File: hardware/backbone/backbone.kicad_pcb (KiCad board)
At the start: 4 copper layers, 31.3 x 68.9 mm, 75 parts, among them J1 M20-7810645R, J140 M20-7810645R, J2 FROM_PREVIOUS, J3 M20-7810645R, J4 SM04B-SRSS-TB(LF)(SN), J5 FH12-24S-0.5SH(55), J9 TO NEXT, Q2 AO3401A, U1 ESP32-S3-WROOM-1_1U_FlexyPin_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, U2 SN65HVD230DR, U3 HC-TYPE-C-16P-01A, U4 TPS562201DDCR, U8 G3VM-61VY3

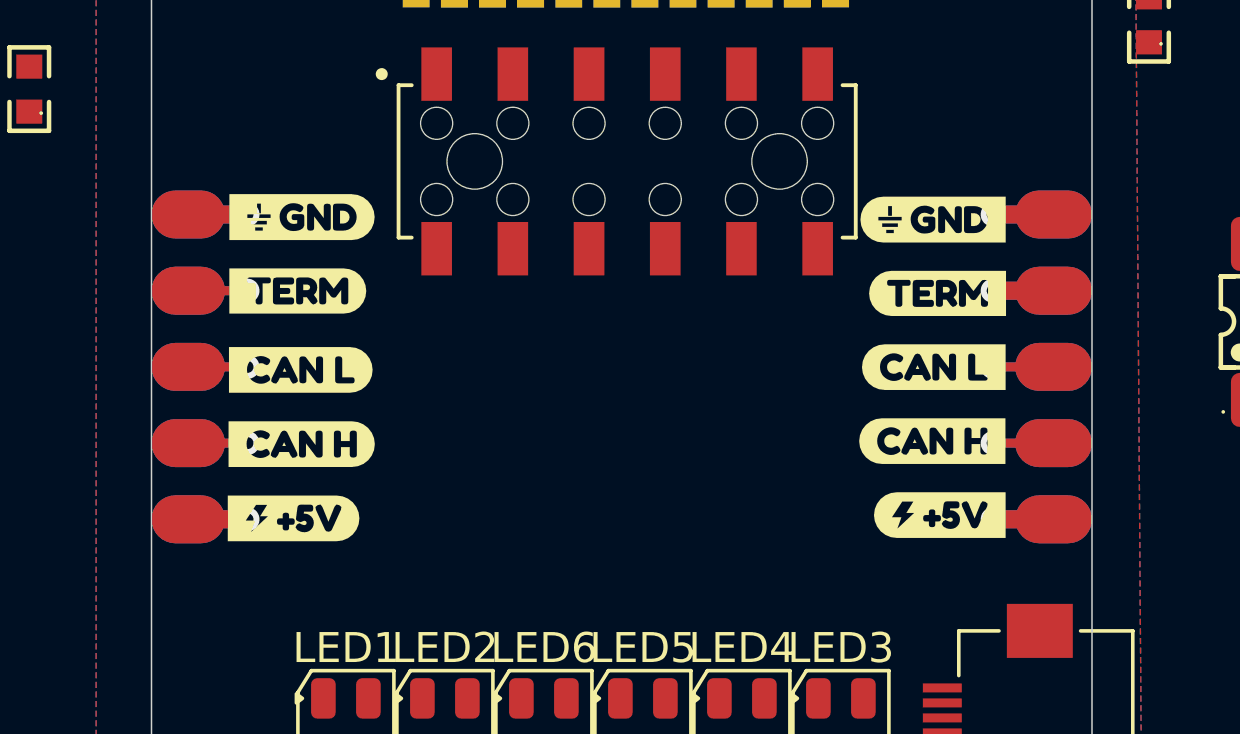
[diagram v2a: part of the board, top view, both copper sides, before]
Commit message: Reinforce magnetic connector power and ground layer transitions
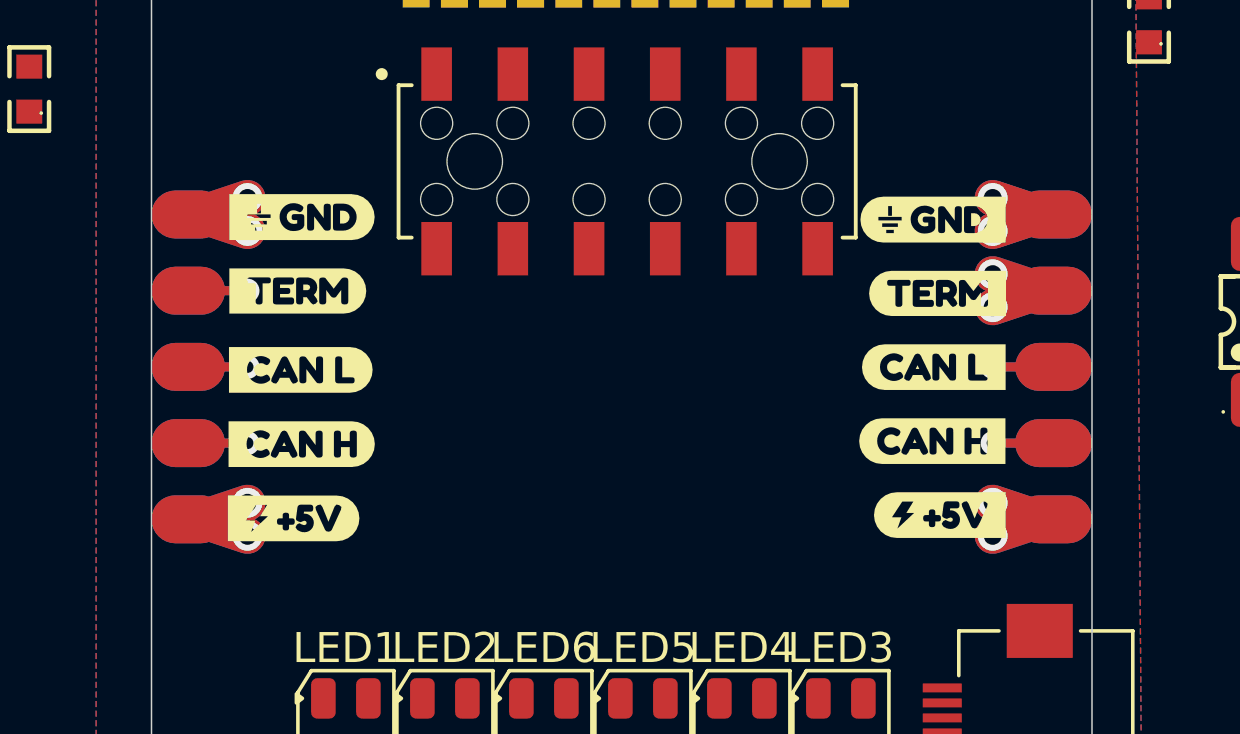
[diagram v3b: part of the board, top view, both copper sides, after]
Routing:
- net 5V: track 9.90 -> 20.9 mm, vias 3 -> 6
- net GND: track 6.60 -> 13.9 mm, vias 2 -> 4
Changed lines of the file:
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@@
 (footprint "Resistor_SMD:R_0603_1608Metric" (layer "F.Cu") (descr "Resistor SMD 0603 (1608 Metric), square (rectangular) end terminal, IPC-7351 nominal, (Body size source: IPC-SM-782 page 72, https://www.pcb-3d.com/wordpress/wp-content/uploads/ipc-sm-782a_amendment_1_and_2.pdf)") (tags "resistor") (property "Reference" "R36" (at 0 -1.43 0) (layer "F.SilkS") (effects (font (size 1 1) (thickness 0.15)))) (property "Value" "33k 1%" (at 0 1.43 0) (layer "F.Fab") (effects (font (size 1 1) (thickness 0.15))) (hide yes)) (property "KiLib_Generator" "SMD_2terminal_chip_molded" (at 0 0 0) (layer "F.SilkS") (hide yes) (effects (font (size 1 1) (thickness 0.15)))) (attr smd) (duplicate_pad_numbers_are_jumpers no) (fp_line (start -0.237258 -0.5225) (end 0.237258 -0.5225) (stroke (width 0.12) (type solid)) (layer "F.SilkS")) (fp_line (start -0.237258 0.5225) (end 0.237258 0.5225) (stroke (width 0.12) (type solid)) (layer "F.SilkS")) (fp_rect (start -1.48 -0.73) (end 1.48 0.73) (stroke (width 0.05) (type solid)) (fill no) (layer "F.CrtYd")) (fp_rect (start -0.8 -0.4125) (end 0.8 0.4125) (stroke (width 0.1) (type solid)) (fill no) (layer "F.Fab")) (fp_text user "${REFERENCE}" (at 0 0 0) (layer "F.Fab") (effects (font (size 0.4 0.4) (thickness 0.06)))) (pad "1" smd roundrect (at -0.825 0) (size 0.8 0.95) (layers "F.Cu" "F.Mask" "F.Paste") (roundrect_rratio 0.25) (net "VCORE")) (pad "2" smd roundrect (at 0.825 0) (size 0.8 0.95) (layers "F.Cu" "F.Mask" "F.Paste") (roundrect_rratio 0.25) (net "Net-(U4-VFB)")) (embedded_fonts no) (model "${KICAD10_3DMODEL_DIR}/Resistor_SMD.3dshapes/R_0603_1608Metric.step" (offset (xyz 0 0 0)) (scale (xyz 1 1 1)) (rotate (xyz 0 0 0))) (at 243 86) (property "MPN" "0603WAF3302T5E" (at 0 0 0) (layer "F.Fab") (hide yes) (effects (font (size 1 1) (thickness 0.15)))) (property "LCSC Part" "C4216" (at 0 0 0) (layer "F.Fab") (hide yes) (effects (font (size 1 1) (thickness 0.15)))))
 (footprint "Resistor_SMD:R_0603_1608Metric" (layer "F.Cu") (descr "Resistor SMD 0603 (1608 Metric), square (rectangular) end terminal, IPC-7351 nominal, (Body size source: IPC-SM-782 page 72, https://www.pcb-3d.com/wordpress/wp-content/uploads/ipc-sm-782a_amendment_1_and_2.pdf)") (tags "resistor") (property "Reference" "R37" (at 0 -1.43 0) (layer "F.SilkS") (effects (font (size 1 1) (thickness 0.15)))) (property "Value" "10k 1%" (at 0 1.43 0) (layer "F.Fab") (effects (font (size 1 1) (thickness 0.15))) (hide yes)) (property "KiLib_Generator" "SMD_2terminal_chip_molded" (at 0 0 0) (layer "F.SilkS") (hide yes) (effects (font (size 1 1) (thickness 0.15)))) (attr smd) (duplicate_pad_numbers_are_jumpers no) (fp_line (start -0.237258 -0.5225) (end 0.237258 -0.5225) (stroke (width 0.12) (type solid)) (layer "F.SilkS")) (fp_line (start -0.237258 0.5225) (end 0.237258 0.5225) (stroke (width 0.12) (type solid)) (layer "F.SilkS")) (fp_rect (start -1.48 -0.73) (end 1.48 0.73) (stroke (width 0.05) (type solid)) (fill no) (layer "F.CrtYd")) (fp_rect (start -0.8 -0.4125) (end 0.8 0.4125) (stroke (width 0.1) (type solid)) (fill no) (layer "F.Fab")) (fp_text user "${REFERENCE}" (at 0 0 0) (layer "F.Fab") (effects (font (size 0.4 0.4) (thickness 0.06)))) (pad "1" smd roundrect (at -0.825 0) (size 0.8 0.95) (layers "F.Cu" "F.Mask" "F.Paste") (roundrect_rratio 0.25) (net "Net-(U4-VFB)")) (pad "2" smd roundrect (at 0.825 0) (size 0.8 0.95) (layers "F.Cu" "F.Mask" "F.Paste") (roundrect_rratio 0.25) (net "GND")) (embedded_fonts no) (model "${KICAD10_3DMODEL_DIR}/Resistor_SMD.3dshapes/R_0603_1608Metric.step" (offset (xyz 0 0 0)) (scale (xyz 1 1 1)) (rotate (xyz 0 0 0))) (at 251 86) (property "MPN" "0603WAF1002T5E" (at 0 0 0) (layer "F.Fab") (hide yes) (effects (font (size 1 1) (thickness 0.15)))) (property "LCSC Part" "C25804" (at 0 0 0) (layer "F.Fab") (hide yes) (effects (font (size 1 1) (thickness 0.15)))))
-(via (at 179.940 102.130) (size 0.8) (drill 0.4) (layers "F.Cu" "B.Cu") (net "5V"))
-(segment (start 181.590 102.130) (end 179.940 102.130) (width 0.6) (layer "F.Cu") (net "5V"))
-(segment (start 181.590 102.130) (end 179.940 102.130) (width 0.6) (layer "B.Cu") (net "5V"))
+(via (at 179.940 101.58) (size 1.0) (drill 0.6) (layers "F.Cu" "B.Cu") (net "5V"))
+(segment (start 181.590 102.130) (end 179.940 101.58) (width 1.2) (layer "F.Cu") (net "5V"))
+(segment (start 181.590 102.130) (end 179.940 101.58) (width 1.2) (layer "B.Cu") (net "5V"))
 (via (at 179.940 99.590) (size 0.8) (drill 0.4) (layers "F.Cu" "B.Cu") (net "CAN_H"))
 (segment (start 181.590 99.590) (end 179.940 99.590) (width 0.3) (layer "F.Cu") (net "CAN_H"))
@@
 (segment (start 181.590 97.050) (end 179.940 97.050) (width 0.3) (layer "F.Cu") (net "CAN_L"))
 (segment (start 181.590 97.050) (end 179.940 97.050) (width 0.3) (layer "B.Cu") (net "CAN_L"))
-(via (at 179.940 94.510) (size 0.8) (drill 0.4) (layers "F.Cu" "B.Cu") (net "5V"))
-(segment (start 181.590 94.510) (end 179.940 94.510) (width 0.6) (layer "F.Cu") (net "5V"))
-(segment (start 181.590 94.510) (end 179.940 94.510) (width 0.6) (layer "B.Cu") (net "5V"))
-(via (at 179.940 91.970) (size 0.8) (drill 0.4) (layers "F.Cu" "B.Cu") (net "GND"))
-(segment (start 181.590 91.970) (end 179.940 91.970) (width 0.6) (layer "F.Cu") (net "GND"))
-(segment (start 181.590 91.970) (end 179.940 91.970) (width 0.6) (layer "B.Cu") (net "GND"))
-(via (at 155.100 102.130) (size 0.8) (drill 0.4) (layers "F.Cu" "B.Cu") (net "5V"))
-(segment (start 153.450 102.130) (end 155.100 102.130) (width 0.6) (layer "F.Cu") (net "5V"))
-(segment (start 153.450 102.130) (end 155.100 102.130) (width 0.6) (layer "B.Cu") (net "5V"))
+(via (at 179.940 93.96) (size 1.0) (drill 0.6) (layers "F.Cu" "B.Cu") (net "5V"))
+(segment (start 181.590 94.510) (end 179.940 93.96) (width 1.2) (layer "F.Cu") (net "5V"))
+(segment (start 181.590 94.510) (end 179.940 93.96) (width 1.2) (layer "B.Cu") (net "5V"))
+(via (at 179.940 91.42) (size 1.0) (drill 0.6) (layers "F.Cu" "B.Cu") (net "GND"))
+(segment (start 181.590 91.970) (end 179.940 91.42) (width 1.2) (layer "F.Cu") (net "GND"))
+(segment (start 181.590 91.970) (end 179.940 91.42) (width 1.2) (layer "B.Cu") (net "GND"))
+(via (at 155.100 101.58) (size 1.0) (drill 0.6) (layers "F.Cu" "B.Cu") (net "5V"))
+(segment (start 153.450 102.130) (end 155.100 101.58) (width 1.2) (layer "F.Cu") (net "5V"))
+(segment (start 153.450 102.130) (end 155.100 101.58) (width 1.2) (layer "B.Cu") (net "5V"))
 (via (at 155.100 99.590) (size 0.8) (drill 0.4) (layers "F.Cu" "B.Cu") (net "CAN_H"))
 (segment (start 153.450 99.590) (end 155.100 99.590) (width 0.3) (layer "F.Cu") (net "CAN_H"))
@@
 (segment (start 153.450 94.510) (end 155.100 94.510) (width 0.3) (layer "F.Cu") (net "TERM_CTRL_OUT"))
 (segment (start 153.450 94.510) (end 155.100 94.510) (width 0.3) (layer "B.Cu") (net "TERM_CTRL_OUT"))
-(via (at 155.100 91.970) (size 0.8) (drill 0.4) (layers "F.Cu" "B.Cu") (net "GND"))
-(segment (start 153.450 91.970) (end 155.100 91.970) (width 0.6) (layer "F.Cu") (net "GND"))
-(segment (start 153.450 91.970) (end 155.100 91.970) (width 0.6) (layer "B.Cu") (net "GND"))
+(via (at 155.100 91.42) (size 1.0) (drill 0.6) (layers "F.Cu" "B.Cu") (net "GND"))
+(segment (start 153.450 91.970) (end 155.100 91.42) (width 1.2) (layer "F.Cu") (net "GND"))
+(segment (start 153.450 91.970) (end 155.100 91.42) (width 1.2) (layer "B.Cu") (net "GND"))
+(via (at 179.940 102.68) (size 1.0) (drill 0.6) (layers "F.Cu" "B.Cu") (net "5V"))
+(segment (start 181.590 102.130) (end 179.940 102.68) (width 1.2) (layer "F.Cu") (net "5V"))
+(segment (start 181.590 102.130) (end 179.940 102.68) (width 1.2) (layer "B.Cu") (net "5V"))
+(via (at 179.940 95.06) (size 1.0) (drill 0.6) (layers "F.Cu" "B.Cu") (net "5V"))
+(segment (start 181.590 94.510) (end 179.940 95.06) (width 1.2) (layer "F.Cu") (net "5V"))
+(segment (start 181.590 94.510) (end 179.940 95.06) (width 1.2) (layer "B.Cu") (net "5V"))
+(via (at 179.940 92.52) (size 1.0) (drill 0.6) (layers "F.Cu" "B.Cu") (net "GND"))
+(segment (start 181.590 91.970) (end 179.940 92.52) (width 1.2) (layer "F.Cu") (net "GND"))
+(segment (start 181.590 91.970) (end 179.940 92.52) (width 1.2) (layer "B.Cu") (net "GND"))
+(via (at 155.100 102.68) (size 1.0) (drill 0.6) (layers "F.Cu" "B.Cu") (net "5V"))
+(segment (start 153.450 102.130) (end 155.100 102.68) (width 1.2) (layer "F.Cu") (net "5V"))
+(segment (start 153.450 102.130) (end 155.100 102.68) (width 1.2) (layer "B.Cu") (net "5V"))
+(via (at 155.100 92.52) (size 1.0) (drill 0.6) (layers "F.Cu" "B.Cu") (net "GND"))
+(segment (start 153.450 91.970) (end 155.100 92.52) (width 1.2) (layer "F.Cu") (net "GND"))
+(segment (start 153.450 91.970) (end 155.100 92.52) (width 1.2) (layer "B.Cu") (net "GND"))
 )
